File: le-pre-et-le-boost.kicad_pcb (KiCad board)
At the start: 2 copper layers, 14.1 x 9.9 mm, 17 parts, among them J1 Power In, J2 IN, J3 OUT, Q1 MMBFJ201, Q2 MMBT5088

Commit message: git.io URL on back silkscreen
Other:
- board text added: "git.io/JJWBx"
- board text removed: "git.io/JJWBn"
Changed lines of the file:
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@@
     )
   )
-  (gr_text "git.io/JJWBn" (at 141.5288 104.4956 90) (layer "B.SilkS")
+  (gr_text "git.io/JJWBx" (at 141.5288 104.4956 90) (layer "B.SilkS")
     (effects (font (size 0.5 0.6) (thickness 0.125)) (justify mirror))
   )

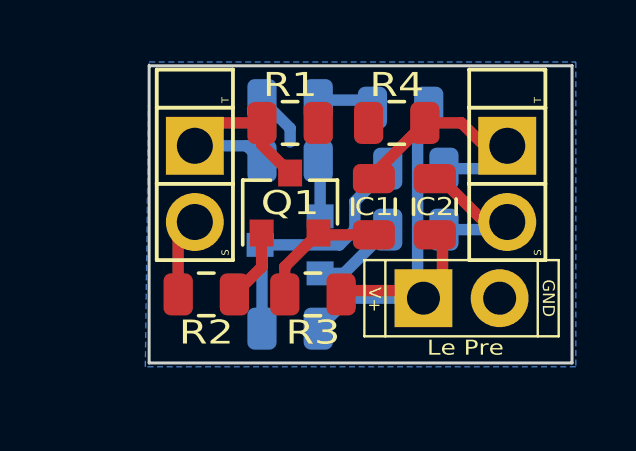
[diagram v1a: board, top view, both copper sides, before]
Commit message: some position and silkscreen adjustments
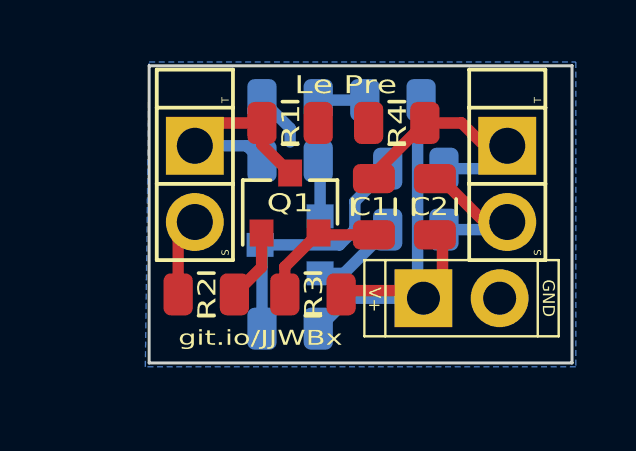
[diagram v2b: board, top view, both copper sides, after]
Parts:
- moved R5 0.36 mm to (143.0, 100.3)
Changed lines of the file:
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@@
       (outputformat 1)
       (mirror false)
-      (drillshape 1)
+      (drillshape 0)
       (scaleselection 1)
-      (outputdirectory "")
+      (outputdirectory "Gerber/")
     )
   )
@@
   )
   (module "Resistor_SMD:R_0805_2012Metric" (layer "B.Cu")
-    (at 143.256 100.584 180)
+    (at 143.002 100.33 180)
     (descr "Resistor SMD 0805 (2012 Metric), square (rectangular) end terminal, IPC_7351 nominal, (Body size source: https://docs.google.com/spreadsheets/d/1BsfQQcO9C6DZCsRaXUlFlo91Tg2WpOkGARC1WS5S8t0/edit?usp=sharing), generated with kicad-footprint-generator")
     (tags "resistor")
@@
     (attr smd)
     (fp_text reference "Q1" (at 0 0 180) (layer "F.SilkS")
-      (effects (font (size 0.8 1) (thickness 0.15)))
+      (effects (font (size 0.6 0.8) (thickness 0.127)))
     )
     (fp_text value "MMBFJ201" (at 0 2.5 90) (layer "F.Fab")
@@
     (tags "resistor")
     (attr smd)
-    (fp_text reference "R4" (at 0 1.27) (layer "F.SilkS")
-      (effects (font (size 0.8 1) (thickness 0.15)))
+    (fp_text reference "R4" (at -0.0254 -0.1016 90) (layer "F.SilkS")
+      (effects (font (size 0.6 0.8) (thickness 0.127)))
     )
     (fp_text value "51k" (at 0 1.65) (layer "F.Fab")
@@
     (tags "resistor")
     (attr smd)
-    (fp_text reference "R3" (at 0 -1.27) (layer "F.SilkS")
-      (effects (font (size 0.8 1) (thickness 0.15)))
+    (fp_text reference "R3" (at -0.0254 -0.0762 90) (layer "F.SilkS")
+      (effects (font (size 0.6 0.8) (thickness 0.127)))
     )
     (fp_text value "6k8" (at 0 1.65) (layer "F.Fab")
@@
     (tags "resistor")
     (attr smd)
-    (fp_text reference "R2" (at 0 -1.27) (layer "F.SilkS")
-      (effects (font (size 0.8 1) (thickness 0.15)))
+    (fp_text reference "R2" (at -0.0254 -0.127 90) (layer "F.SilkS")
+      (effects (font (size 0.6 0.8) (thickness 0.127)))
     )
     (fp_text value "2k2" (at 0 1.65) (layer "F.Fab")
@@
     (tags "resistor")
     (attr smd)
-    (fp_text reference "R1" (at 0 -1.27) (layer "F.SilkS")
-      (effects (font (size 0.8 1) (thickness 0.127)))
+    (fp_text reference "R1" (at 0.0254 0.1016 270) (layer "F.SilkS")
+      (effects (font (size 0.6 0.8) (thickness 0.125)))
     )
     (fp_text value "3M" (at 0 1.65) (layer "F.Fab")
@@
     (tags "capacitor")
     (attr smd)
-    (fp_text reference "C2" (at 0 0 180) (layer "F.SilkS")
-      (effects (font (size 0.6 0.7) (thickness 0.15)))
+    (fp_text reference "C2" (at 0 -0.1778 180) (layer "F.SilkS")
+      (effects (font (size 0.6 0.7) (thickness 0.127)))
     )
     (fp_text value "10u" (at 0 1.65 90) (layer "F.Fab")
@@
     (tags "capacitor")
     (attr smd)
-    (fp_text reference "C1" (at 0 0) (layer "F.SilkS")
-      (effects (font (size 0.6 0.7) (thickness 0.15)))
+    (fp_text reference "C1" (at 0 -0.127) (layer "F.SilkS")
+      (effects (font (size 0.6 0.7) (thickness 0.127)))
     )
     (fp_text value "4u7" (at 0 1.65 90) (layer "F.Fab")
@@
     )
   )
-  (gr_text "git.io/JJWBx" (at 141.5288 104.4956 90) (layer "B.SilkS")
-    (effects (font (size 0.5 0.6) (thickness 0.125)) (justify mirror))
-  )
-  (gr_text "Le Pre" (at 145.415 108.585) (layer "F.SilkS")
-    (effects (font (size 0.5 0.6) (thickness 0.125)))
-  )
-  (gr_text "${REVISION}" (at 136.525 107.95) (layer "B.SilkS")
-    (effects (font (size 0.6 0.6) (thickness 0.127)) (justify mirror))
-  )
-  (gr_text "${DATE}" (at 147.828 108.6612) (layer "B.SilkS")
+  (gr_text "git.io/JJWBx" (at 138.5824 108.2548) (layer "F.SilkS")
+    (effects (font (size 0.5 0.7) (thickness 0.125)))
+  )
+  (gr_text "Le Pre" (at 141.4272 99.822) (layer "F.SilkS")
+    (effects (font (size 0.6 0.8) (thickness 0.125)))
+  )
+  (gr_text "${REVISION}" (at 136.4742 108.3564) (layer "B.SilkS")
+    (effects (font (size 0.5 0.8) (thickness 0.125)) (justify mirror))
+  )
+  (gr_text "${DATE}" (at 147.9042 108.6104) (layer "B.SilkS")
     (effects (font (size 0.5 0.6) (thickness 0.125)) (justify left mirror))
   )

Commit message: ground fill now specified as single zone applying to both sides
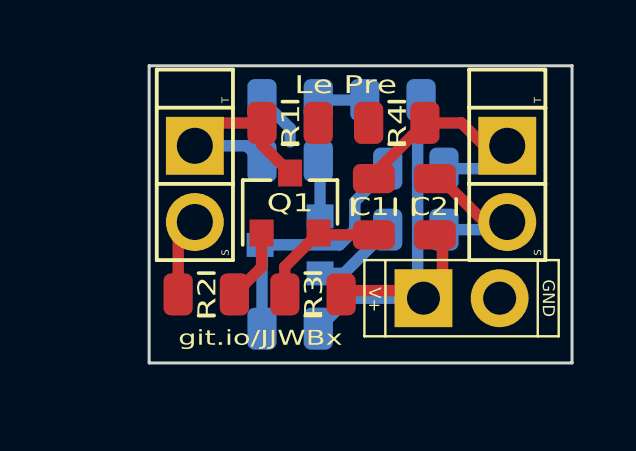
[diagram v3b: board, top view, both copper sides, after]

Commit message: v0.2: THT footprints for electrolytics
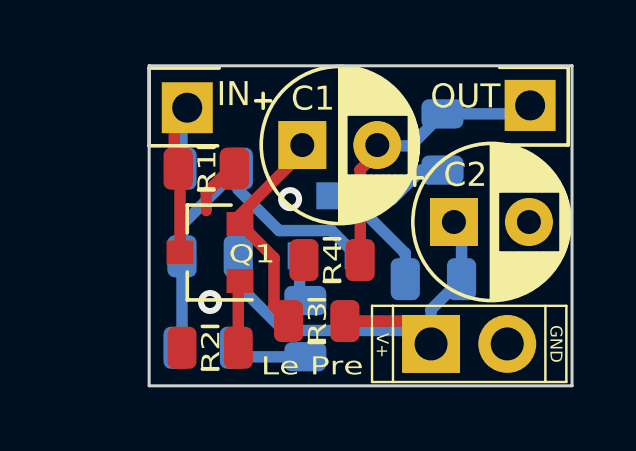
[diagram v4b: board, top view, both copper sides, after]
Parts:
- C1, C2: footprint Capacitor_SMD:C_0805_2012Metric -> Capacitor_THT:CP_Radial_D5.0mm_P2.50mm
- J2, J3: footprint rockola_kicad_footprints:2PADS_TS_Horizontal -> rockola_kicad_footprints:Pin_1x01_P2.54mm
- moved R6 8.72 mm to (136.8, 108.6), turned to 0 degrees
- moved R5 8.02 mm to (136.9, 105.5)
- moved R4 5.06 mm to (141.0, 105.7)
- moved R7 5.05 mm to (144.4, 106.3)
- moved R8 4.95 mm to (140.1, 108.0), turned to -90 degrees
- moved R1 3.18 mm to (136.8, 102.6)
- moved C1 3.15 mm to (140.0, 101.8), turned to 0 degrees
- moved Q1 3.14 mm to (136.9, 105.4), turned to 180 degrees
- moved J3 2.72 mm to (147.6, 100.5), turned to 90 degrees
- moved C3 2.68 mm to (136.9, 102.6)
- moved J2 2.55 mm to (136.1, 100.6)
- moved R2 1.78 mm to (136.9, 108.6)
- moved J1 1.55 mm to (145.5, 109.7)
- moved Q2 1.42 mm to (140.8, 104.5), turned to 90 degrees
- moved C4 1.26 mm to (144.7, 101.7), turned to 90 degrees
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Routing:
- net Net-(C3-Pad2): track 5.82 -> 12.3 mm
- net GND: track 9.97 -> 4.22 mm, vias 0 -> 2
- net Net-(C1-Pad1): track 4.26 -> 7.47 mm
- net Net-(Q2-Pad2): track 2.86 -> 1.55 mm
- net OUT: track 8.36 -> 9.53 mm
- net Net-(C4-Pad1): track 8.67 -> 7.90 mm
- net +9V: track 16.6 -> 16.0 mm
- net Net-(Q1-Pad1): track 2.42 -> 1.87 mm
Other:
- board size 14.1 x 9.9 mm -> 14.1 x 10.7 mm

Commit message: v0.3: separate in/out for both sides
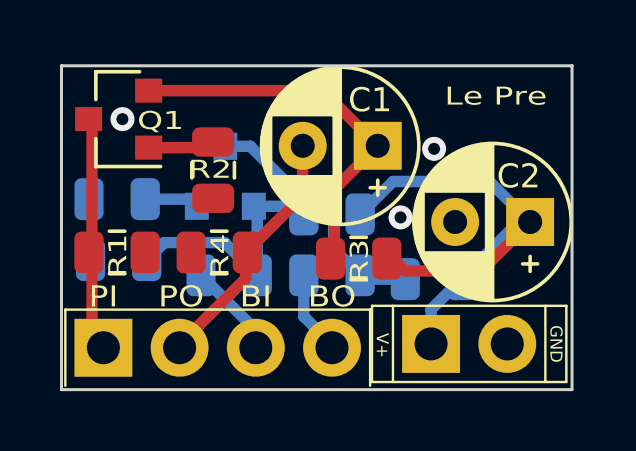
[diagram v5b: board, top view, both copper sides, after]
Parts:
- removed J3: OUT, rockola_kicad_footprints:Pin_1x01_P2.54mm
- C1, C2: footprint Capacitor_THT:CP_Radial_D5.0mm_P2.50mm -> rockola_kicad_footprints:CP_D5.0_P2.50
- J2: value IN -> Conn_01x04_Female; footprint rockola_kicad_footprints:Pin_1x01_P2.54mm -> rockola_kicad_footprints:Stomp_4pin_ALT2
- moved J2 8.07 mm to (137.2, 108.6), turned to 0 degrees
- moved R8 7.62 mm to (133.8, 103.6), turned to 180 degrees
- moved R2 5.92 mm to (137.0, 102.7), turned to -90 degrees
- moved C4 5.77 mm to (141.0, 106.2), turned to 180 degrees
- moved Q1 5.39 mm to (133.9, 101.0)
- moved R5 4.30 mm to (141.0, 104.1)
- moved R6 4.13 mm to (133.9, 105.7), turned to 180 degrees
- moved R1 4.08 mm to (133.8, 105.4)
- moved Q2 3.81 mm to (137.4, 102.9)
- moved R4 3.77 mm to (137.2, 105.4)
- moved C3 3.61 mm to (137.5, 106.2)
- moved C2 2.54 mm to (147.6, 104.4), turned to 180 degrees
- moved C1 2.51 mm to (142.5, 101.9), turned to 180 degrees
- moved R3 2.51 mm to (141.9, 105.6)
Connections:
- C1 pad 2: OUT -> PRE_OUT
- C3 pad 1: IN -> BOOST_IN
- C4 pad 2: OUT -> BOOST_OUT
- J2 pad 1: IN -> PRE_IN
- Q1 pad 3: IN -> PRE_IN
- R1 pad 1: IN -> PRE_IN
- R4 pad 1: OUT -> PRE_OUT
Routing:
- net OUT: track 9.53 -> 0.00 mm
- net PRE_OUT: track 0.00 -> 8.33 mm
- net PRE_IN: track 0.00 -> 7.72 mm
- net IN: track 6.93 -> 0.00 mm
- net Net-(C1-Pad1): track 7.47 -> 12.7 mm
- net GND: track 4.22 -> 0.00 mm, vias 2 -> 3
- net Net-(C3-Pad2): track 12.3 -> 8.51 mm
- net BOOST_IN: track 0.00 -> 3.07 mm
- net BOOST_OUT: track 0.00 -> 2.70 mm
- net +9V: track 16.0 -> 17.9 mm
- net Net-(C4-Pad1): track 7.90 -> 8.86 mm
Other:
- board size 14.1 x 10.7 mm -> 17 x 10.8 mm
- board text added: "B"
- board text added: "BI"
- board text added: "BO"
- board text added: "I"
- board text added: "O"
- board text added: "P"
- board text added: "PI"
- board text added: "PO"
